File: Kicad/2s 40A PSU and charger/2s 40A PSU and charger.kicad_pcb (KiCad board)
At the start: 4 copper layers, 45 x 20 mm, 102 parts, among them J1 Keystone 3579, J10 USB_C_Receptacle_USB2.0_16P, J11 1.27mm 4 pin socket, J12 USB, J2 JST XH-S Balance Plug, J3 Keystone 3579, J4 Keystone 3569, J5 Keystone 3569, J6 Keystone 3579, J7 Keystone 3579, J8 Keystone 3569, J9 Keystone 3569, Q1 PJA3430, Q2 PJA3430, Q3 Vishay sir404dp, or SiR500DP, Q4 PJA3430, Q5 PJA3430, Q6 Vishay sir404dp, or SiR500DP, U1 BQ76905RGRR, U2 AP63203WU, U3 BQ24780SRUYR, U4 TLV709A33DBVR, U5 THVD1420DRLR, U6 CH32X035G8U6

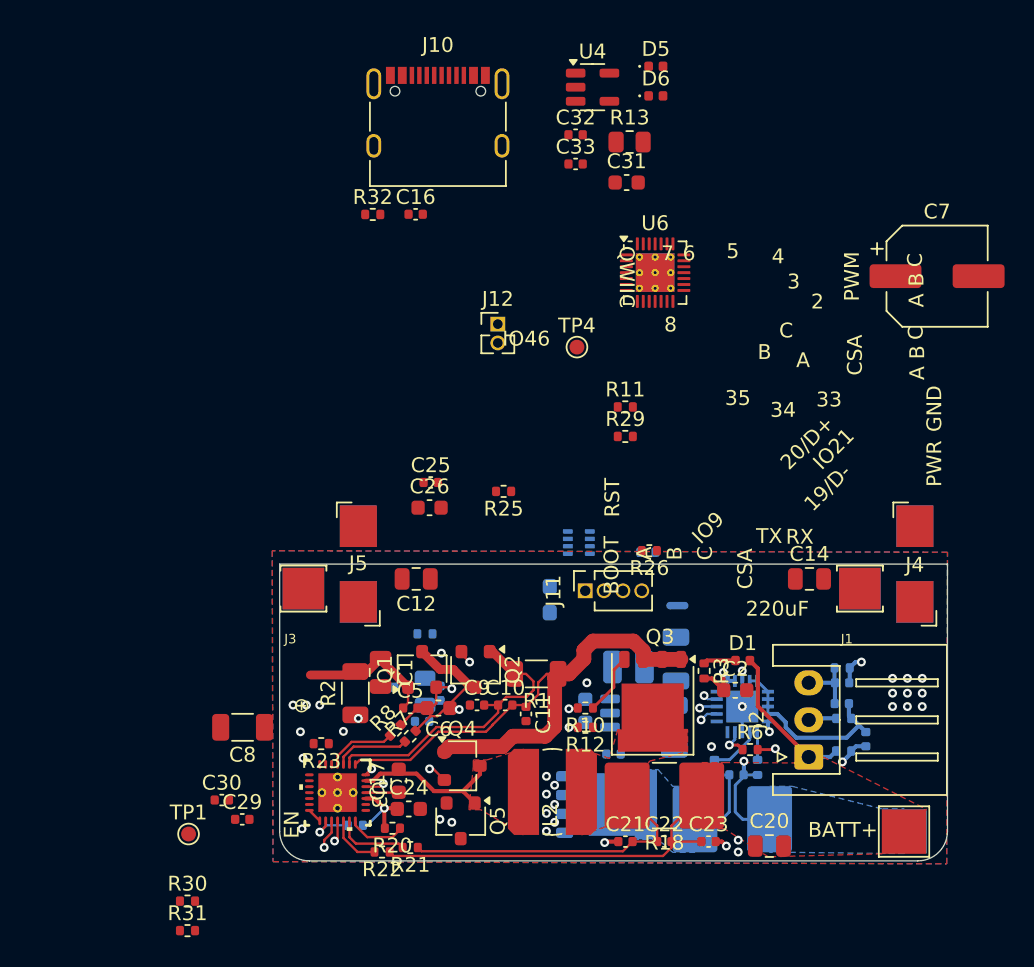
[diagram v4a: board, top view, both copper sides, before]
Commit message: Add proper ESD protection and pulldowns for USB-C
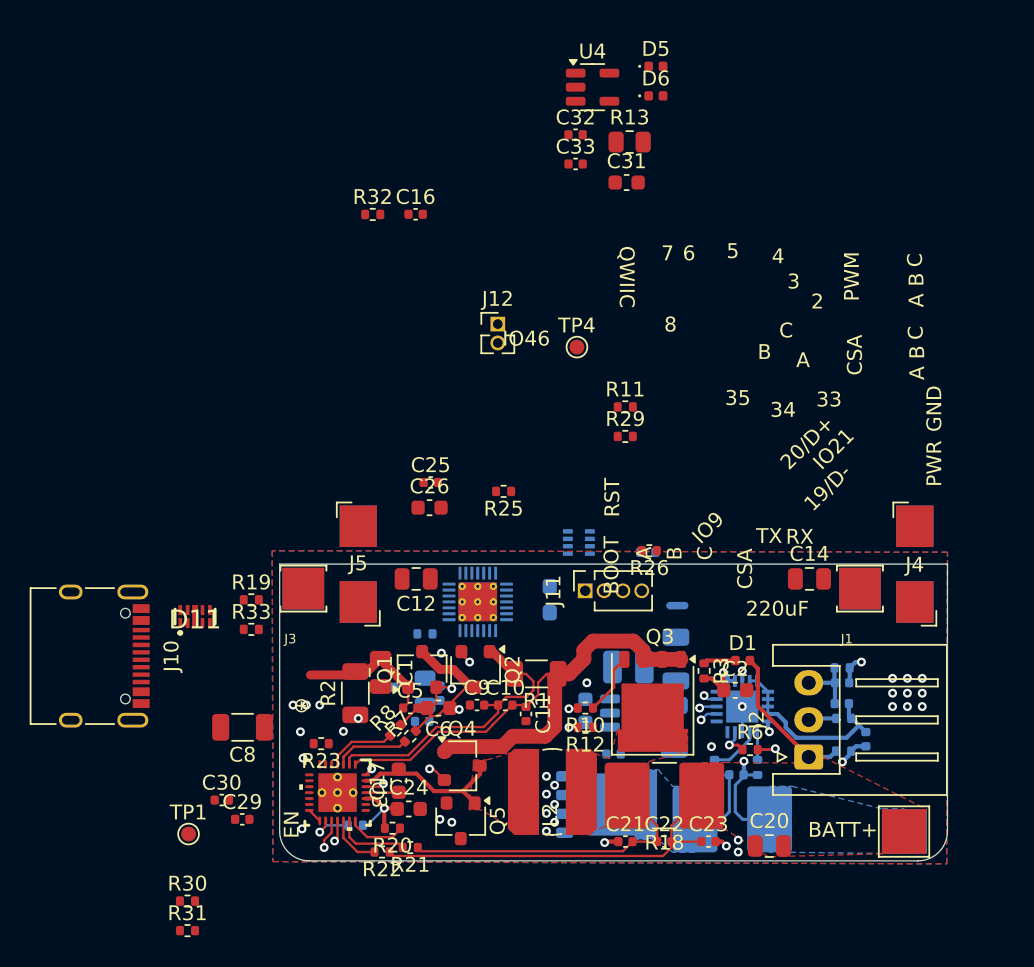
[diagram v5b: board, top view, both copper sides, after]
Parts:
- removed C7: 220uF,APA0609221M016R, Capacitor_SMD:CP_Elec_6.3x9.9
- added D11: CDDFN10-3324P, CDDFN10-3324P:CDDFN103324P, F.Cu at (102.4, 115.9)
- added R19: 5.1k, Resistor_SMD:R_0402_1005Metric, F.Cu at (106.2, 114.4)
- added R33: 5.1k, Resistor_SMD:R_0402_1005Metric, F.Cu at (106.2, 116.4)
- U6: moved to B.Cu
- moved J10 42.6 mm to (95.1, 118.2), turned to -90 degrees
- moved U6 25.2 mm to (121.5, 114.5), turned to 180 degrees

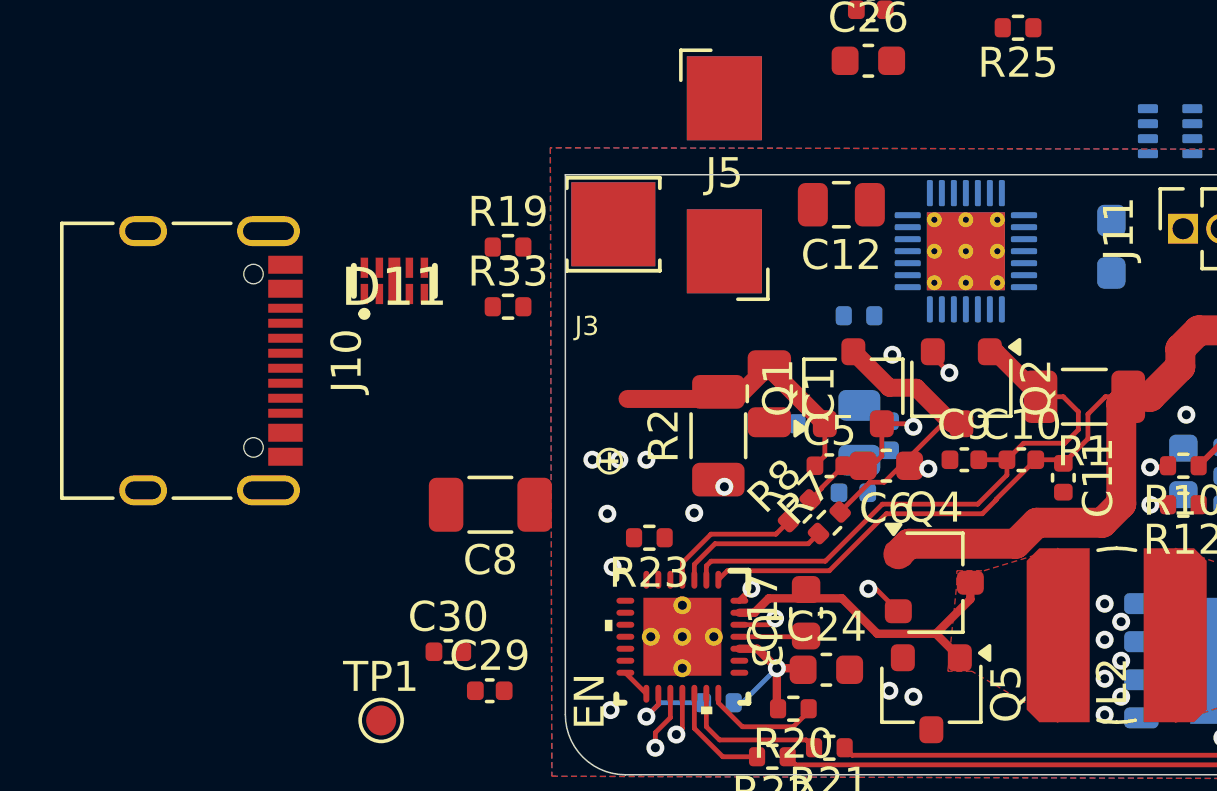
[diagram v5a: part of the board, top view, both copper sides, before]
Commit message: Updated Ground connections and tweaked some formatting
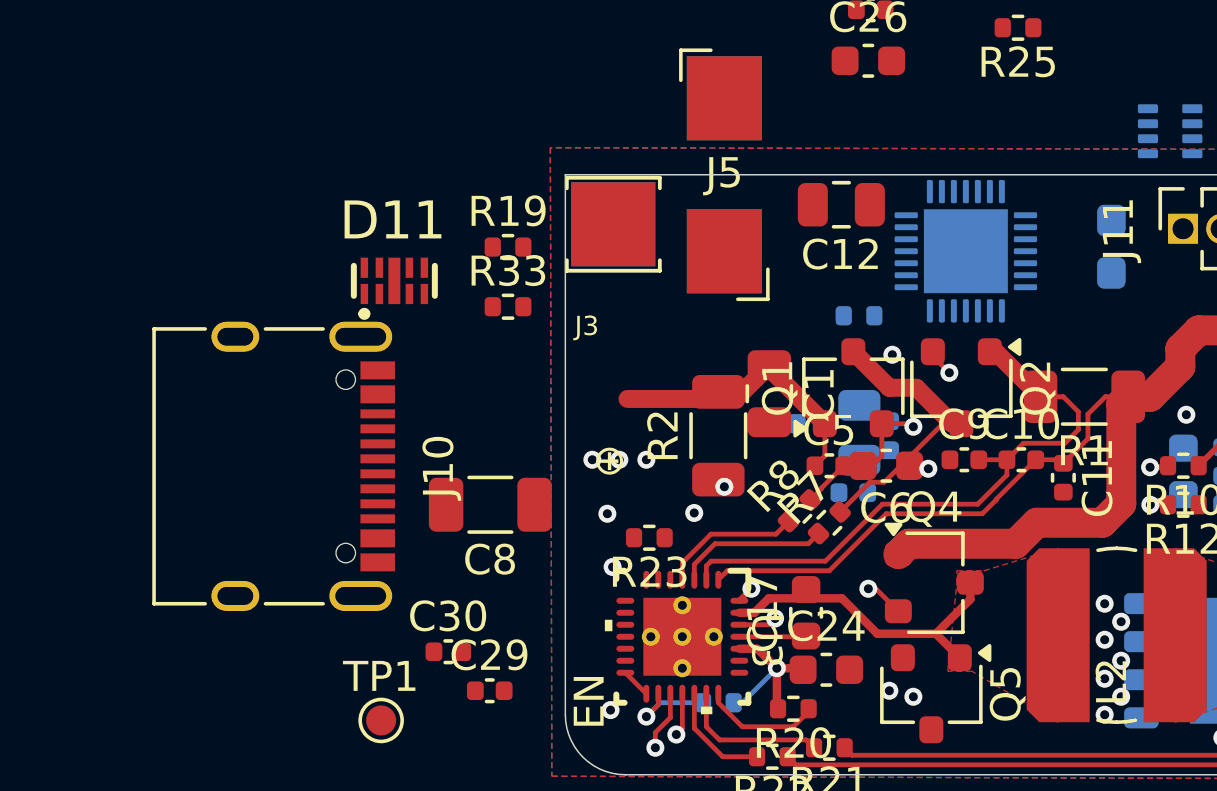
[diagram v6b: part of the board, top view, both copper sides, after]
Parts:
- U6: footprint Package_DFN_QFN:QFN-28-1EP_4x4mm_P0.4mm_EP2.6x2.6mm_ThermalVias -> Package_DFN_QFN:QFN-28-1EP_4x4mm_P0.4mm_EP2.8x2.8mm
- moved J10 4.67 mm to (98.2, 121.7)
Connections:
- C33 pad 2: GNDPWR -> GND
- D11 pad 10: /Connectors/D+ -> /Connectors/CC1
- D11 pad 3: GNDPWR -> GND
- D11 pad 6: /Connectors/CC1 -> /Connectors/D+
- D11 pad 7: /Connectors/CC2 -> /Connectors/D-
- D11 pad 8: GNDPWR -> GND
- D11 pad 9: /Connectors/D- -> /Connectors/CC2
- R19 pad 1: GNDPWR -> GND
- R33 pad 1: GNDPWR -> GND

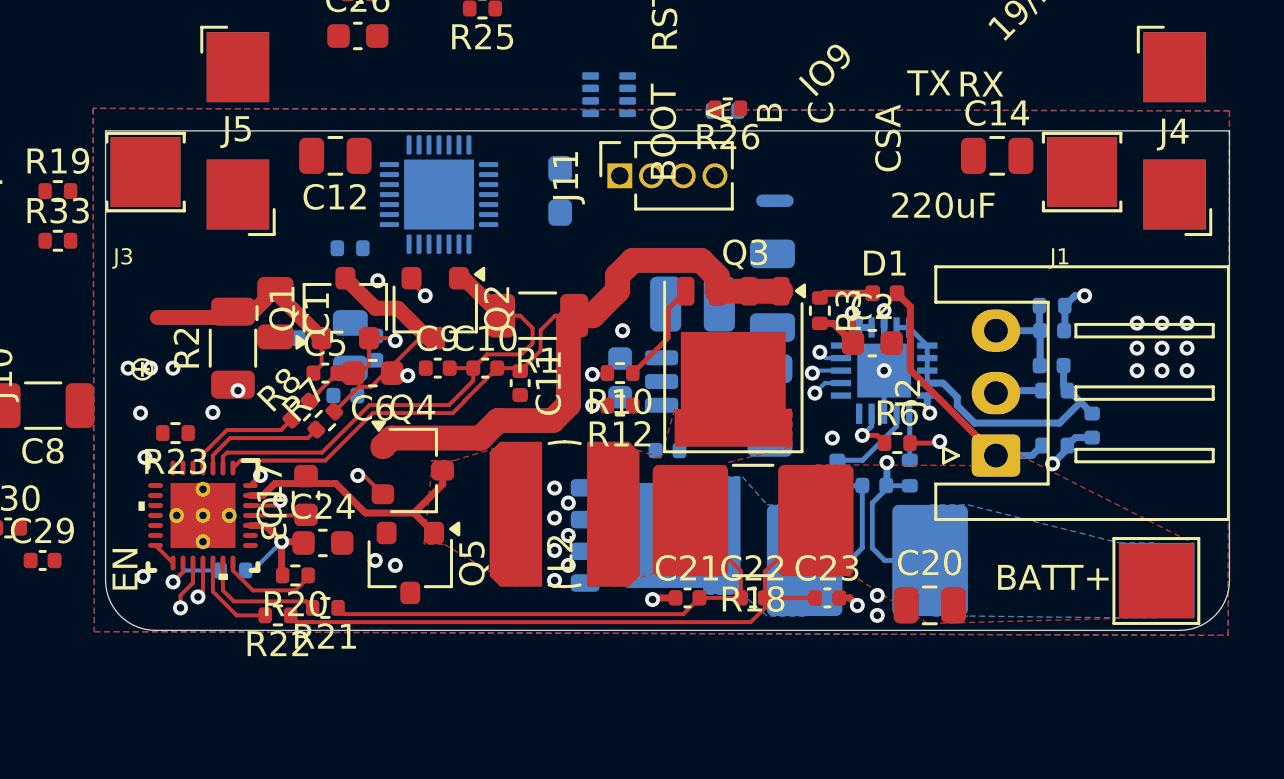
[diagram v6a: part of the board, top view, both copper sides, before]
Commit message: Added use of Net Class Directives to speed up routing
I don't have to manually change wire sizes now
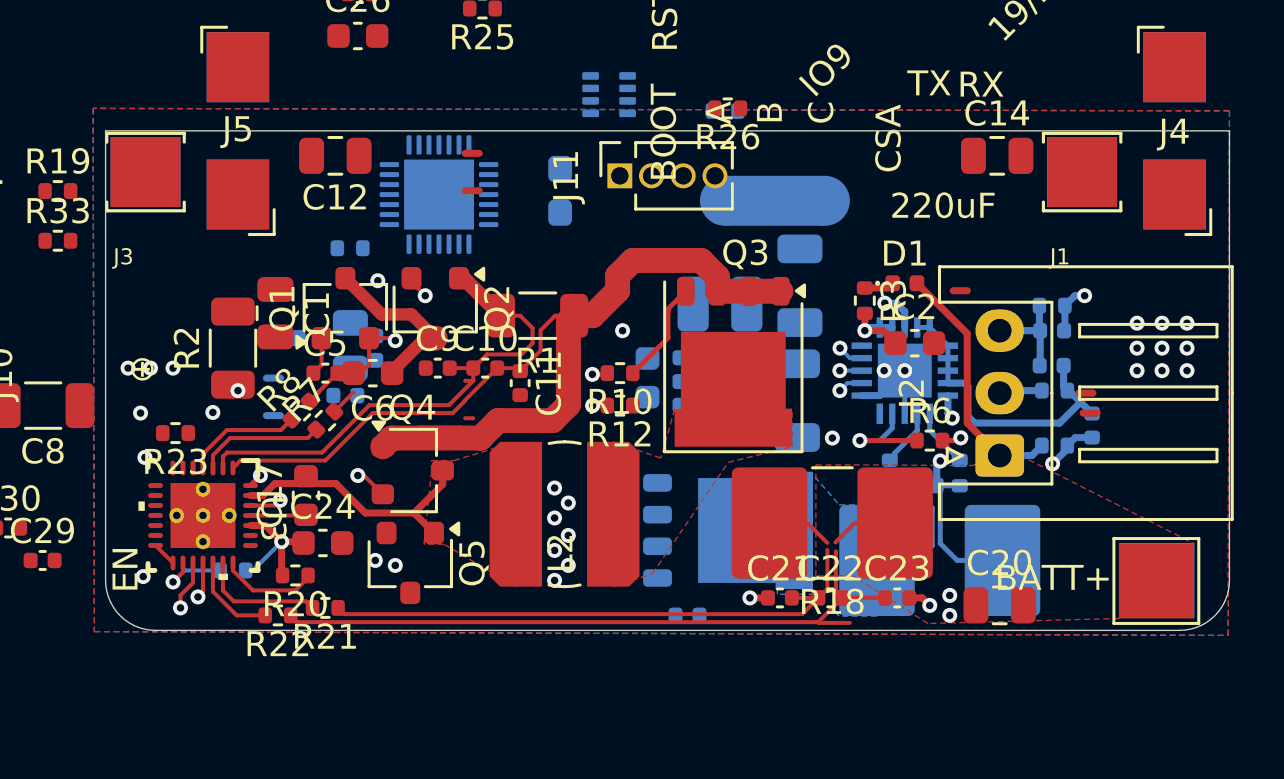
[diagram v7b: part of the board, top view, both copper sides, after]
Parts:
- added NT10: PWR NetTie, custom_Connector:NetTie-2_SMD_Pad0.28mm, F.Cu at (122.8, 112.9)
- added NT11: PWR NetTie, custom_Connector:NetTie-2_SMD_Pad0.28mm, F.Cu at (122.8, 114.4)
- added NT12: PWR NetTie, custom_Connector:NetTie-2_SMD_Pad0.28mm, B.Cu at (114.8, 121.9)
- added NT13: PWR NetTie, custom_Connector:NetTie-2_SMD_Pad0.28mm, B.Cu at (114.8, 123.4)
- added NT14: Sense NetTie, custom_Connector:NetTie-2_SMD_Pad0.16mm, F.Cu at (117.9, 122.6)
- added NT2: Sense NetTie, custom_Connector:NetTie-2_SMD_Pad0.16mm, F.Cu at (122.7, 122.0)
- added NT3: Sense NetTie, custom_Connector:NetTie-2_SMD_Pad0.16mm, F.Cu at (122.7, 123.5)
- added NT4: Charge NetTie, custom_Connector:NetTie-2_SMD_Pad0.8mm, F.Cu at (121.5, 124.2)
- added NT5: Sense NetTie, custom_Connector:NetTie-2_SMD_Pad0.16mm, F.Cu at (137.3, 129.0)
- added NT6: Sense NetTie, custom_Connector:NetTie-2_SMD_Pad0.16mm, F.Cu at (137.0, 128.9)
- added NT7: PWR NetTie, custom_Connector:NetTie-2_SMD_Pad0.28mm, F.Cu at (147.3, 122.5)
- added NT8: PWR NetTie, custom_Connector:NetTie-2_SMD_Pad0.28mm, F.Cu at (147.5, 123.3)
- added NT9: PWR NetTie, custom_Connector:NetTie-2_SMD_Pad0.28mm, F.Cu at (142.3, 118.4)
- NT1: value NetTie_2 -> Main GND NetTie; footprint NetTie:NetTie-2_SMD_Pad0.5mm -> NetTie:NetTie-2_SMD_Pad2.0mm
- moved C4 6.65 mm to (131.4, 131.4)
- moved C21 3.70 mm to (135.1, 130.7)
- moved R18 3.17 mm to (137.2, 127.7)
- moved C22 3.10 mm to (137.1, 130.7)
- moved Q6 2.91 mm to (132.9, 128.0)
- moved R14 2.90 mm to (141.5, 129.2)
- moved C20 2.80 mm to (143.9, 131.0)
- moved C23 2.80 mm to (139.8, 130.7)
- moved R5 2.10 mm to (139.5, 125.7)
- moved C3 2.02 mm to (140.9, 126.2)
- moved R4 2.00 mm to (142.3, 125.7)
- moved R3 1.84 mm to (138.5, 118.8)
- moved C2 1.70 mm to (140.5, 120.5)
- moved R6 1.30 mm to (141.1, 124.4)
- moved C28 1.12 mm to (135.8, 122.8)
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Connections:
- C10 pad 1: Net-(Q2-D) -> Net-(U3-ACP)
- C10 pad 2: /Battery Charger/MOTORPWR -> Net-(U3-ACN)
- C11 pad 1: /Battery Charger/MOTORPWR -> Net-(U3-ACN)
- C18 pad 2: /Battery Balancer/BAT- -> Net-(C18-Pad2)
- C19 pad 2: /Battery Balancer/BAT- -> Net-(C18-Pad2)
- C20 pad 2: /Battery Balancer/BAT+ -> /Battery Balancer/+BAT
- C21 pad 2: Net-(Q3-S) -> Net-(C21-Pad2)
- C22 pad 1: Net-(Q3-S) -> Net-(C21-Pad2)
- C22 pad 2: /Battery Balancer/BAT+ -> Net-(C22-Pad2)
- C23 pad 1: /Battery Balancer/BAT+ -> Net-(C22-Pad2)
- C3 pad 1: /Battery Balancer/BAT- -> /Battery Balancer/-BAT
- C9 pad 2: Net-(Q2-D) -> Net-(U3-ACP)
- D1 pad 2: /Battery Balancer/BAT+ -> Net-(D1-A)
- D2 pad 2: /Battery Charger/IN -> Net-(D2-A)
- D3 pad 2: /Battery Balancer/BAT+ -> Net-(D3-A)
- D5 pad 2: /Battery Charger/IN -> Net-(D5-A)
- D6 pad 2: /Battery Balancer/BAT+ -> Net-(D6-A)
- H1 pad 1: /Battery Balancer/BAT+ -> /Battery Balancer/+BAT
- H2 pad 1: /Battery Balancer/BAT- -> /Battery Balancer/-BAT
- J2 pad 1: /Battery Balancer/BAT+ -> /Battery Balancer/+BAT
- J2 pad 3: /Battery Balancer/BAT- -> /Battery Balancer/-BAT
- Q4 pad 1: /Battery Charger/MOTORPWR -> Net-(Q4-D)
- R14 pad 2: /Battery Balancer/BAT- -> /Battery Balancer/-BAT
- R15 pad 2: /Battery Balancer/BAT+ -> Net-(NT8-Pad1)
- R17 pad 2: /Battery Balancer/BAT- -> Net-(C18-Pad2)
- R18 pad 1: /Battery Balancer/BAT+ -> /Battery Balancer/+BAT
- R21 pad 1: Net-(Q3-S) -> Net-(C21-Pad2)
- R22 pad 1: /Battery Balancer/BAT+ -> Net-(C22-Pad2)
- R30 pad 2: /Battery Balancer/BAT+ -> /Battery Balancer/+BAT
- R4 pad 2: /Battery Balancer/BAT- -> /Battery Balancer/-BAT
- R7 pad 2: Net-(Q1-S) -> Net-(NT14-Pad1)
- U3 pad 1: /Battery Charger/MOTORPWR -> Net-(U3-ACN)
- U3 pad 2: Net-(Q2-D) -> Net-(U3-ACP)
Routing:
- net /Battery Balancer/BAT+: track 36.0 -> 0.00 mm
- net Net-(C22-Pad2): track 0.00 -> 27.3 mm
- net /Battery Balancer/BAT-: track 27.0 -> 0.00 mm, vias 1 -> 0
- net Net-(C18-Pad2): track 0.00 -> 25.6 mm, vias 0 -> 1
- net Net-(C21-Pad2): track 0.00 -> 22.4 mm
- net Net-(Q3-S): track 20.4 -> 2.64 mm
- net (no net): track 0.00 -> 10.3 mm
- net /Battery Charger/IN: track 9.49 -> 1.68 mm
- net Net-(Q1-S): track 9.85 -> 7.06 mm
- net /Battery Balancer/+BAT: track 0.00 -> 2.72 mm
- net Net-(U1-DSG): track 2.04 -> 4.37 mm
- net GNDPWR: track 1.80 -> 3.94 mm, vias 29 -> 30
- net /Battery Balancer/Up: track 15.7 -> 16.9 mm
- net Net-(U1-SRN): track 3.44 -> 2.32 mm
- net Net-(D1-K): track 2.19 -> 1.19 mm
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- added copper zone on F.Cu, net /Battery Balancer/+BAT
- removed copper zone on F.Cu, net /Battery Balancer/BAT+
- removed copper zone on B.Cu, net /Battery Balancer/BAT-
